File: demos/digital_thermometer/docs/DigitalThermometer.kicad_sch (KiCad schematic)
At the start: 1 part

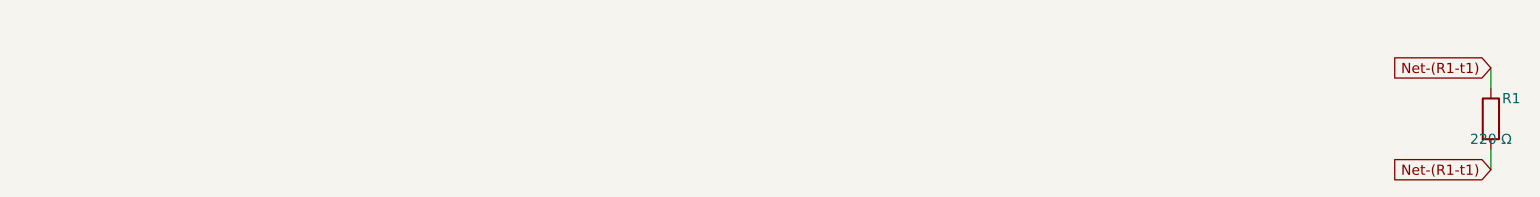
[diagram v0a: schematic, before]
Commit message: export: kicad_sch — Phase 2.5b: layered placement, wire routing, KiCad 10 compatibility (#23)
* export: kicad_sch — Phase 2.5b: layered placement + routing + KiCad 9 fix

Placement (placement.py, complete rewrite):
- Replaces naive grid with Layered Signal Flow algorithm (spec §5 stages 1–8)
- Stage 1: band classification — power chips/rails at top, LEDs at bottom,
  everything else in the signal band
- Stage 2: signal-flow DAG via BFS from Rail/Connector sources; layer = BFS
  distance from nearest source
- Stage 3–4: place within (band, layer) cells at 1500-mil (38.1 mm) same-band
  spacing, 1000-mil inter-band gutter, 25.4 mm page margin
- Stage 6: cluster breakup — up to 10 iterations shifting same-band parts
  that land closer than 0.9× SAME_BAND_SPACING_MM
- Stage 8: page sized to fit (A4 → A3 → A2 → A1)
- grid_place() and sheet_size_mm() kept as shims for backward-compat

Routing (routing.py, new file):
- route_net(): connects stub ends with Manhattan L-shapes (horizontal first)
- find_junctions(): returns points where ≥3 wire endpoints coincide
- renderer uses routed wires between signal-net stub ends

Hierarchical (hierarchical.py, new file):
- collect_boards(), is_multi_board(), sub_sheet_filename() — interface stub
  for multi-Board sub-sheet emission (full implementation deferred)

KiCad 9 sub-symbol name fix (library_loader.py):
- KiCad 9 schematics expect sub-symbols nested inside their parent in
  lib_symbols to use the bare name (R_0_1, LED_0_1, 4069_1_0) — NOT the
  lib-qualified name (Device:R_0_1, Device:LED_0_1, 4xxx:4069_1_0)
- Fixed _qualify_names() to add the lib: prefix only to the exact parent
  symbol name using a lookahead (?=") that prevents sub-unit names from
  being qualified

Tests (+25 tests):
- test_placement.py: band classification, all-on-grid, determinism,
  minimum spacing, power < signal < indicator Y ordering, page sizing
- test_routing.py: H/V segments, L-shapes, orthogonality, grid snap,
  junction detection

Golden files re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
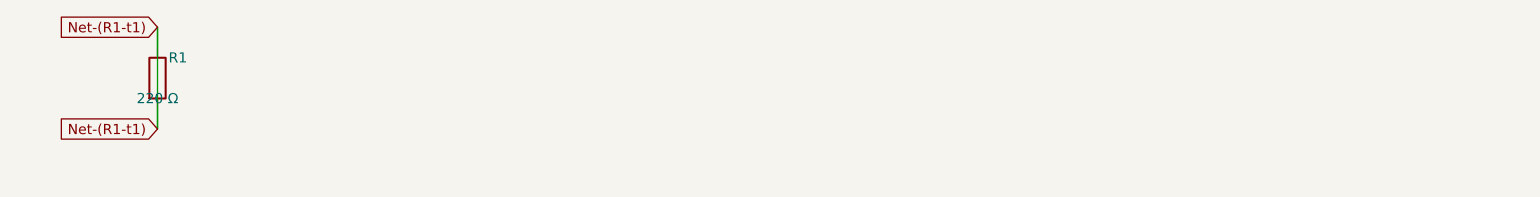
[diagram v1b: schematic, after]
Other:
- moved on the sheet: R1
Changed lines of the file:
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@@
 (kicad_sch
-  (version 20240618)
+  (version 20250114)
   (generator "wirebench")
-  (generator_version "0.1")
-  (paper "A3")
+  (generator_version "0.2")
+  (paper "A4")
   (symbol
     (lib_id "Device:R")
-    (at 229.87 30.48 0)
+    (at 63.5 25.4 0)
     (unit 1)
     (exclude_from_sim no)
@@
     (dnp no)
     (property "Reference" "R1"
-      (at 232.41 27.94 0)
+      (at 66.04 22.86 0)
       (effects (font (size 1.27 1.27)))
     )
     (property "Value" "220 Ω"
-      (at 229.87 33.02 0)
+      (at 63.5 27.94 0)
       (effects (font (size 1.27 1.27)))
     )
@@
   )
   (wire
-    (pts (xy 229.87 34.29) (xy 229.87 36.83))
+    (pts (xy 63.5 29.21) (xy 63.5 31.75))
     (stroke (width 0) (type default))
   )
   (global_label "Net-(R1-t1)"
     (shape input)
-    (at 229.87 36.83 0)
+    (at 63.5 31.75 0)
     (fields_autoplaced yes)
     (effects (font (size 1.27 1.27)) (justify right))
@@
   )
   (wire
-    (pts (xy 229.87 26.67) (xy 229.87 24.13))
+    (pts (xy 63.5 21.59) (xy 63.5 19.05))
     (stroke (width 0) (type default))
   )
   (global_label "Net-(R1-t1)"
     (shape input)
-    (at 229.87 24.13 0)
+    (at 63.5 19.05 0)
     (fields_autoplaced yes)
     (effects (font (size 1.27 1.27)) (justify right))
@@
     )
   )
+  (wire
+    (pts (xy 63.5 19.05) (xy 63.5 31.75))
+    (stroke (width 0) (type default))
+  )
   (sheet_instances
